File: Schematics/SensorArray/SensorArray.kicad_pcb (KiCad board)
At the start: 2 copper layers, 36 x 144.2 mm, 30 parts, among them J1 Conn_01x10_MountingPin, Q1 IRLM2502, Q2 IRLM2502, U1 PCA9557PW, U10 ITR8307, U11 ITR8307, U12 ITR8307, U13 ITR8307, U14 ITR8307, U15 ITR8307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

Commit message: Uploaded V1.0 of PCB
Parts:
- added REF**: OSHW-Logo2_7.3x6mm_SilkScreen, Symbol:OSHW-Logo2_7.3x6mm_SilkScreen, F.Cu at (138.0, 89.0)
- added REF**: KiCad-Logo2_5mm_SilkScreen, Symbol:KiCad-Logo2_5mm_SilkScreen, F.Cu at (138.0, 129.9)
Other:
- board text added: "Marrajo Morro - v1.0 By: LabGluon www.twitch.tv/labgluon"

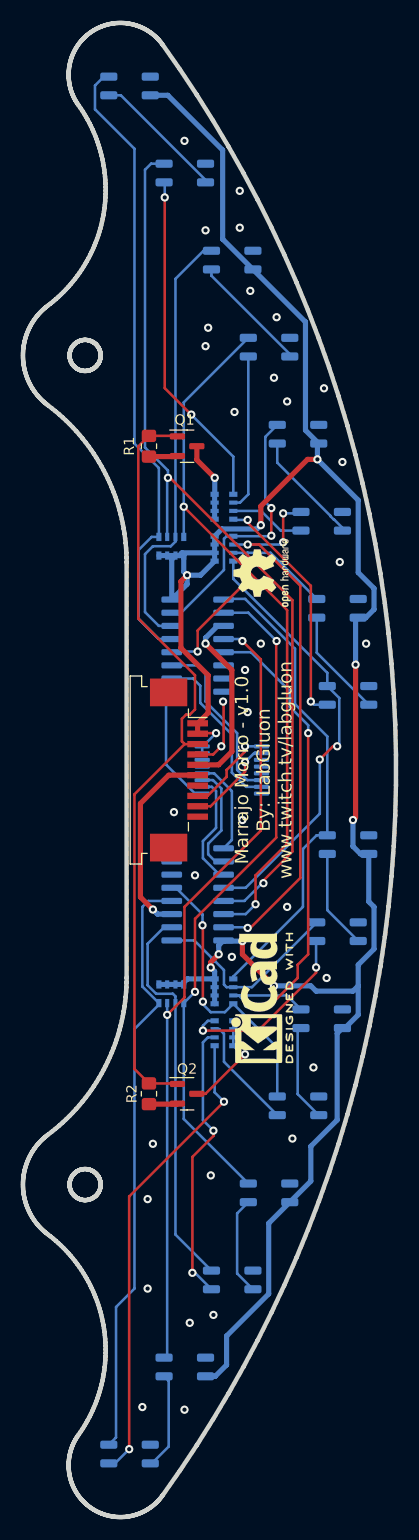
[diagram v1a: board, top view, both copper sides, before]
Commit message: Version 1.1 PCB: Fixed I2C pullups
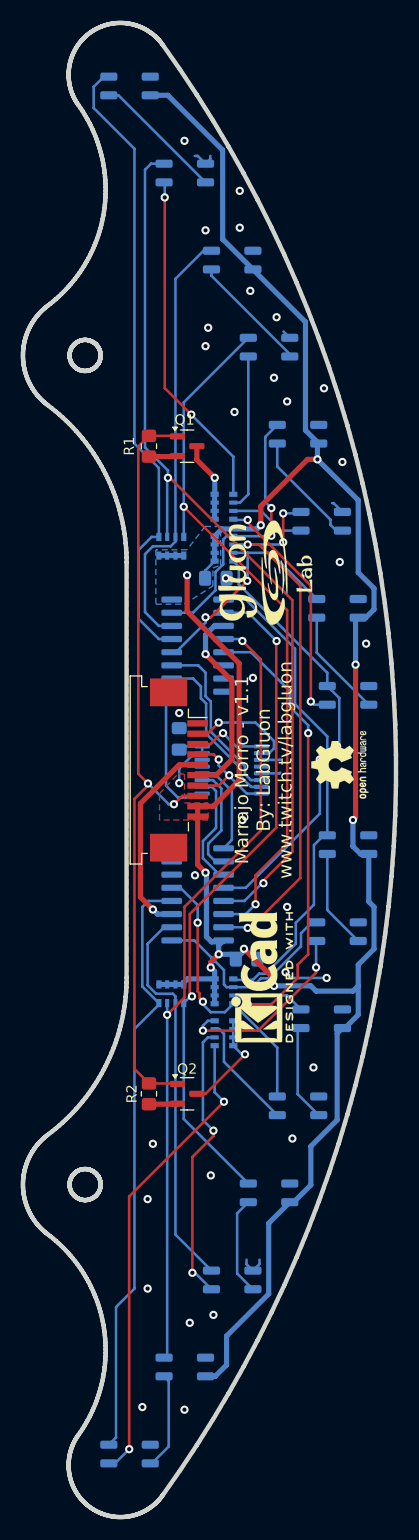
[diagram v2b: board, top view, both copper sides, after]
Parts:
- added C1: 22u, Capacitor_SMD:C_0805_2012Metric_Pad1.18x1.45mm_HandSolder, B.Cu at (130.0, 105.0)
- added C2: 22u, Capacitor_SMD:C_0805_2012Metric_Pad1.18x1.45mm_HandSolder, B.Cu at (133.6, 89.5)
- added C3: 22u, Capacitor_SMD:C_0805_2012Metric_Pad1.18x1.45mm_HandSolder, B.Cu at (136.5, 126.2)
- added G***: LOGO, GluonLib:LogoGluon_12mm, F.Cu at (138.0, 89.0)
- U10, U11, U12, U13, U14, U15, U16, U17, U18, U19, U4, U5, U6, U7, U8, U9: footprint GluonLib:Everlight_ITR1201SR10AR -> OptoDevice:Everlight_ITR1201SR10AR
- moved REF** 20.0 mm to (145.5, 107.5)
- moved REF** 2.00 mm to (138.0, 128.0)
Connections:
- J1 pad 1: +3V3 -> unconnected-(J1-Pin_1-Pad1)
- J1 pad 10: unconnected-(J1-Pin_10-Pad10) -> +3V3
- J1 pad 2: +3V3 -> SDA
- J1 pad 3: MOSFET_PWM -> SCL
- J1 pad 5: V1 -> V2
- J1 pad 6: V2 -> V1
- J1 pad 8: SCL -> MOSFET_PWM
- J1 pad 9: SDA -> +3V3
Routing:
- net GND: track 12.6 -> 32.3 mm, vias 36 -> 35
- net +3V3: track 228.6 -> 242.8 mm, vias 10 -> 11
- net SDA: track 8.83 -> 10.7 mm
- net SCL: track 8.84 -> 7.13 mm
- net Net-(U1-IO2): track 11.9 -> 13.4 mm
- net LineSensor8: track 46.4 -> 47.6 mm
- net V1: track 18.1 -> 19.1 mm
- net LineSensor6: track 24.0 -> 23.1 mm
- net LineSensor9: track 19.3 -> 20.0 mm
- net LineSensor4: track 25.9 -> 26.5 mm
- net MOSFET_PWM: track 75.4 -> 76.0 mm, vias 0 -> 2
- added copper zone on B.Cu, net +3V3
- added copper zone on F.Cu, net +3V3
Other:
- board text added: "Marrajo Morro - v1.1 By: LabGluon www.twitch.tv/labgluon"
- board text removed: "Marrajo Morro - v1.0 By: LabGluon www.twitch.tv/labgluon"
